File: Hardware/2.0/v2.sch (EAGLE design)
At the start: 63 parts, among them IC1 LM386N-1, IC3 PCF8563, IC5 7805TV, IC9 TL074P, K1 SRD-5VDC-SL-C, K2 SRD-5VDC-SL-C, K3 SRD-5VDC-SL-C, K4 SRD-5VDC-SL-C, Q4 32768 hz, T1 BC639, T2 BC639, T3 BC639, T4 BC639

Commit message: poczatki pracy nad v2.0
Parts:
- removed C11, C14: 100n, rcl:C-EUC1206
- removed C13: 220n, rcl:C-EU050-025X075
- removed D1, D2, D3, D4: 1N4148, diode:1N4004
- removed IC2: (no value), ads11xx:ADS1110
- removed IC9: TL074P, linear:TL074P
- removed JP2: Wej audio, pinhead:PINHD-1X2
- removed JP5: BATERY_OFF, jumper:JP1E
- removed JP6: Elektroda_Ph, pinhead:PINHD-1X2
- removed K1, K2, K3, K4: SRD-5VDC-SL-C, relay:ZF112
- removed R1, R2, R3, R4: 470, rcl:R-EU_0204/7
- removed R11, R12: 4,7k, my_library:R-EU_0207/10
- removed R16: 470, my_library:R-EU_0207/10
- removed R25: 0R, rcl:R-EU_R1206
- removed R26: 50k, rcl:R-TRIMM64X
- removed R30, R31: 220k, rcl:R-EU_R1206
- removed R32, R36: 10k, rcl:R-EU_R1206
- removed R33, R34: 4k7, rcl:R-EU_R1206
- removed R35: 1k, rcl:R-TRIMM64X
- removed T1, T2, T3, T4: BC639, transistor:BC639-NPN-TO92-ECB
- removed X1, X2, X3, X4: (no value), con-wago-500:W237-103
- added AU_IN: Wej audio, pinhead:PINHD-1X2
- added AU_OUT: Glosnik, pinhead:PINHD-1X2
- added IC4: ULN2803A, uln-udn:ULN2803A
- added R10: 470, rcl:R-EU_R1206
- added R8, R9: 4,7k, rcl:R-EU_R1206
- added X5: (no value), con-subd:M09H
- JP3: value Glosnik -> (none); device pinhead:PINHD-1X2 -> pinhead:PINHD-1X5/90
- R5: device rcl:R-EU_0207/7 -> rcl:R-EU_R1206
- R6: device rcl:R-EU_0204/7 -> rcl:R-EU_R1206
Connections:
- removed net N$100: C11.2, R30.2, R31.1
- removed net N$102: C14.1, IC9B.+IN, R31.2
- removed net N$104: C11.1, IC9B.-IN, IC9B.OUT, R25.2
- removed net N$109: IC9C.-IN, R33.2, R34.2
- removed net N$110: IC9C.OUT, R32.2, R33.1
- removed net N$12: R2.1, T2.B
- removed net N$13: D3.A, K21.2, T3.C
- removed net N$14: K12.P, X3-2.KL
- removed net N$15: K12.S, X3-3.KL
- removed net N$16: K12.O, X3-1.KL
- removed net N$17: R3.1, T3.B
- removed net N$19: K22.P, X2-2.KL
- removed net N$20: K22.S, X2-3.KL
- removed net N$21: K22.O, X2-1.KL
- removed net N$23: JP1.18, R3.2
- removed net N$25: D4.A, K41.2, T4.C
- removed net N$26: R4.1, T4.B
- removed net N$28: K42.P, X4-2.KL
- removed net N$29: K42.S, X4-3.KL
- removed net N$31: K42.O, X4-1.KL
- removed net N$32: JP1.22, R4.2
- removed net N$46: C13.1, IC9A.+IN, JP6.2
- removed net N$47: IC9D.+IN, R35.E, R35.S, R36.2
- removed net N$5: R1.1, T1.B
- removed net N$51: IC9C.+IN, R25.1
- removed net N$94: IC9D.-IN, R26.A, R32.1
- removed net N$96: IC9A.-IN, IC9A.OUT, R30.1
- removed net PHOUT: IC2.VIN+, IC9D.OUT, R26.E, R26.S
- new net N$37: IC4.O1, X5.5
- new net N$39: IC4.O3, X5.4
- new net N$40: IC4.O4, X5.8
- new net N$41: IC4.O5, X5.3
- new net N$42: IC4.O6, X5.7
- new net N$49: IC4.I2, JP1.11
- net +12V: now also IC4.CD+, JP3.1, X5.6
- net +5V: now also JP3.2, R8.2, R9.2; no longer D1.C, D2.C, D3.C, D4.C, IC2.VDD, K11.1, K21.1, K31.1, K41.1, R11.1, R12.1, R36.1
- net GND: now also AU_IN.1, AU_OUT.1, IC4.GND, JP3.3, R10.1, X5.1; no longer C13.2, C14.2, IC2.GND, IC2.VIN-, JP2.1, JP3.1, JP6.1, R16.2, R34.1, R35.A, T1.E, T2.E, T3.E, T4.E
- net N$1: now also IC4.I3, JP1.13; no longer JP1.12, R1.2
- net N$10: now also IC4.I6, JP1.18; no longer D2.A, K11.2, T2.C
- net N$2: now also IC4.I4, JP1.16; no longer D1.A, K31.2, T1.C
- net N$22: now also IC4.O2, X5.9; no longer C6.+, D6.C, IC3.VDD, JP5.2
- net N$24: now also C6.+, D6.C, IC3.VDD; no longer JP5.1
- net N$3: now also IC4.I1, JP1.12; no longer JP1.16, R2.2
- net N$33: now also R10.2; no longer R16.1
- net N$6: now also IC4.O7, X5.2; no longer K32.P, X1-2.KL
- net N$61: now also AU_OUT.2; no longer JP3.2
- net N$64: now also AU_IN.2; no longer JP2.2
- net N$7: now also IC4.I7, JP1.22; no longer K32.S, X1-3.KL
- net N$8: now also IC4.I5, JP1.15; no longer K32.O, X1-1.KL
- net SCL: now also JP3.4, R9.1; no longer IC2.SCL, R12.2
- net SDA: now also JP3.5, R8.1; no longer IC2.SDA, R11.2
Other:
- note added: "Imax: 500mA per pin"
- note removed: "pH-Metr"
- moved on the sheet: 12V_INPUT, BAT1, C1, C16, C17, C18, C2, C3, C6, C7, D5, D6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

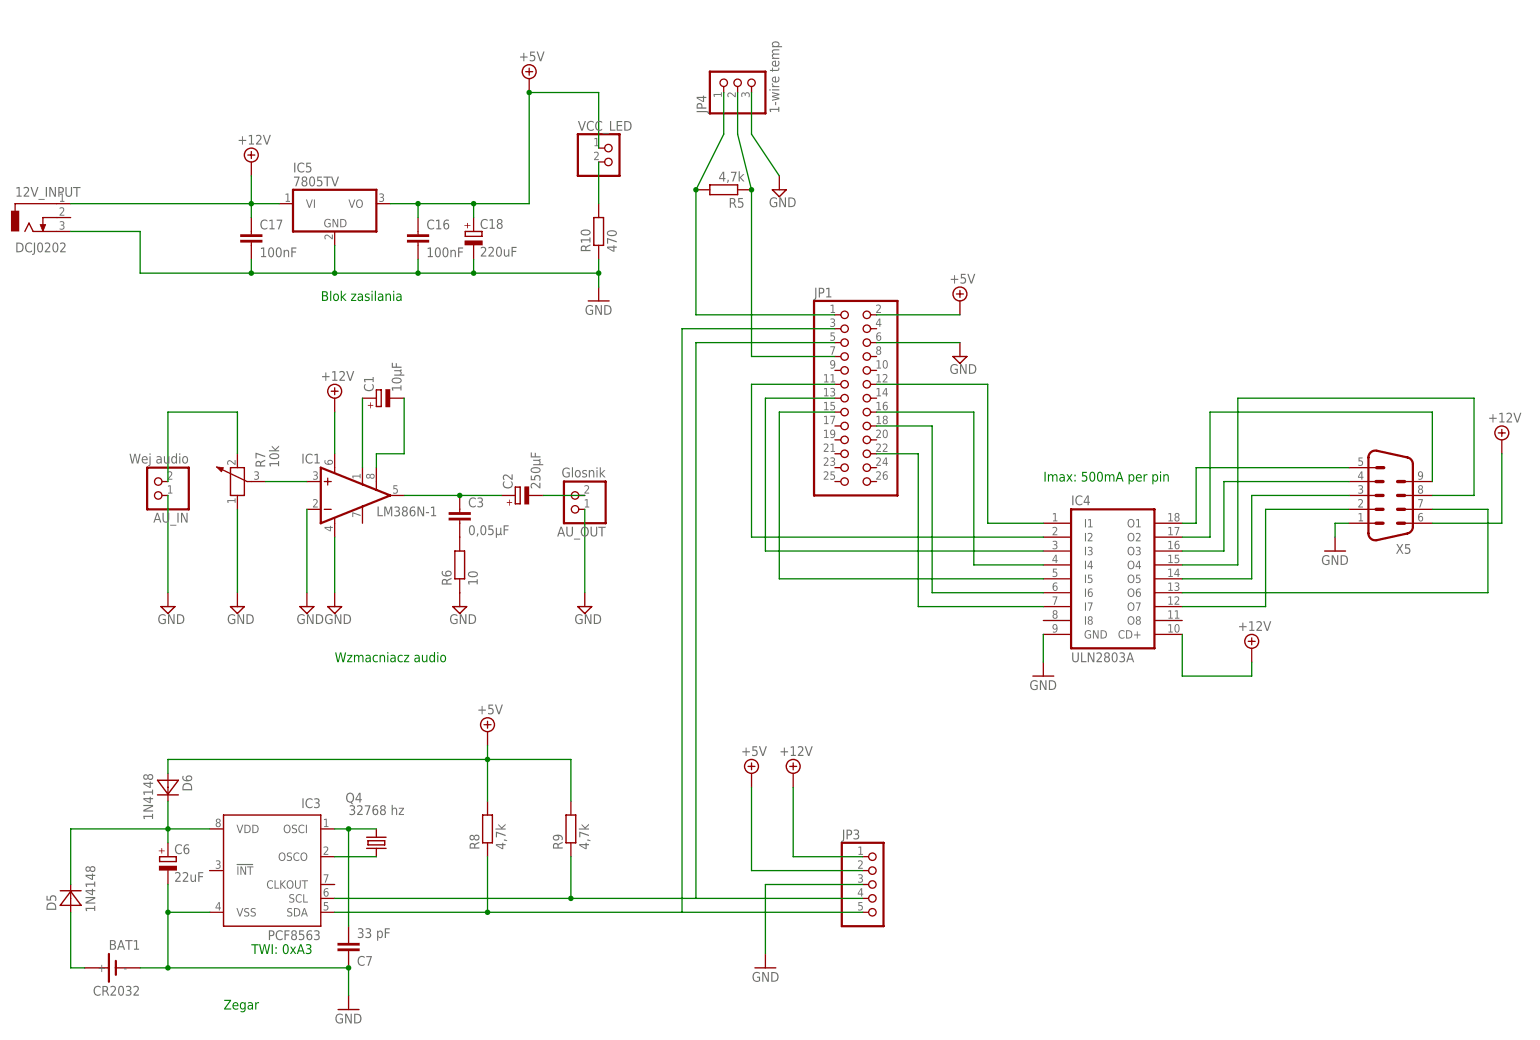
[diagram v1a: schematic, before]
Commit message: - uproszczenie & wersja gotowa do testów
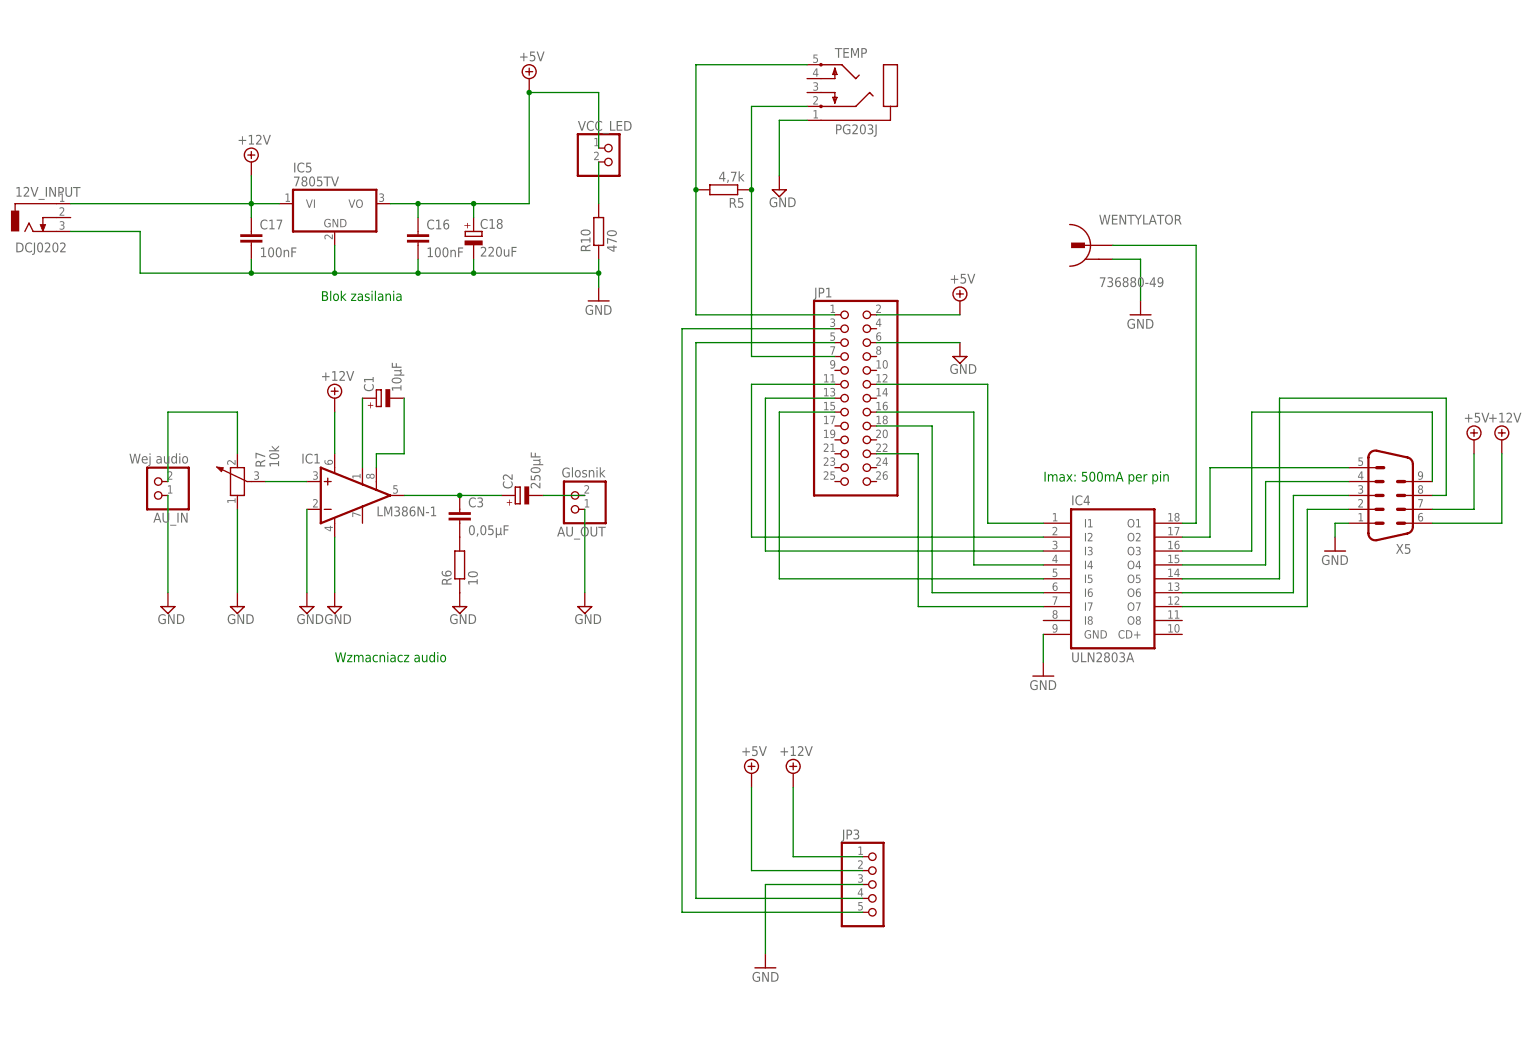
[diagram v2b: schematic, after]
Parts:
- removed BAT1: CR2032, sn2032:SN2032LISPOL
- removed C6: 22uF, my_library:CPOL-EUE2.5-5
- removed C7: 33 pF, my_library:C-EU050-024X044
- removed D5, D6: 1N4148, my_library:1N4148
- removed IC3: PCF8563, my_library:PCF8563
- removed JP4: 1-wire temp, pinhead:PINHD-1X3
- removed Q4: 32768 hz, my_library:CRYSTALTC26V
- removed R8, R9: 4,7k, rcl:R-EU_R1206
- added TEMP: PG203J, con-hirschmann:PG203J
- added WENTYLATOR: 736880-49, con-conrad:736880-49
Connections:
- removed net N$24: C6.+, D5.C, D6.C, IC3.VDD
- removed net N$27: BAT1.+, D5.A
- removed net N$39: IC4.O3, X5.4
- removed net N$41: IC4.O5, X5.3
- removed net N$42: IC4.O6, X5.7
- new net N$5: IC4.O3, X5.9
- net +12V: no longer IC4.CD+
- net +5V: now also X5.7; no longer D6.A, R8.2, R9.2
- net GND: now also TEMP.1, WENTYLATOR.2; no longer BAT1.-, C6.-, C7.1, IC3.VSS, JP4.3
- net N$11: now also TEMP.5; no longer JP4.1
- net N$18: now also TEMP.2; no longer JP4.2
- net N$22: now also X5.5; no longer X5.9
- net N$37: now also WENTYLATOR.1; no longer X5.5
- net N$4: now also IC4.O6, X5.3; no longer IC3.OSCO, Q4.1
- net N$40: now also X5.4; no longer X5.8
- net N$9: now also IC4.O5, X5.8; no longer C7.2, IC3.OSCI, Q4.2
- net SCL: no longer IC3.SCL, R9.1
- net SDA: no longer IC3.SDA, R8.1
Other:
- note removed: "TWI: 0xA3"
- note removed: "Zegar"
